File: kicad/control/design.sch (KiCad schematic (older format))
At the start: 20 parts, among them CON1 USB-MINI-B, IC1 ATMEGA1284P-P, P1 CONN_LH, P2 CONN_RH, P3 CONN_LT, P4 CONN_RT, P5 CONN_1, P6 CONN_1, SW1 RESET, X1 12 MHz

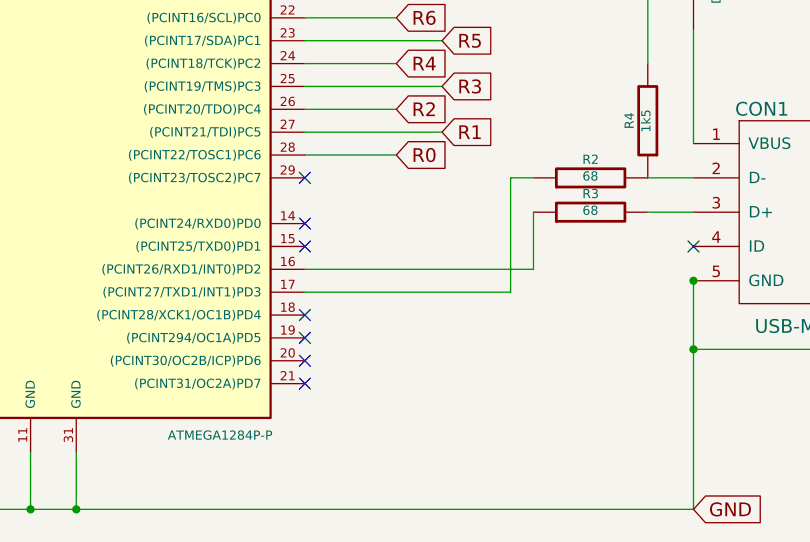
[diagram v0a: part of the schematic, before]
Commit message: adding logo to keypad
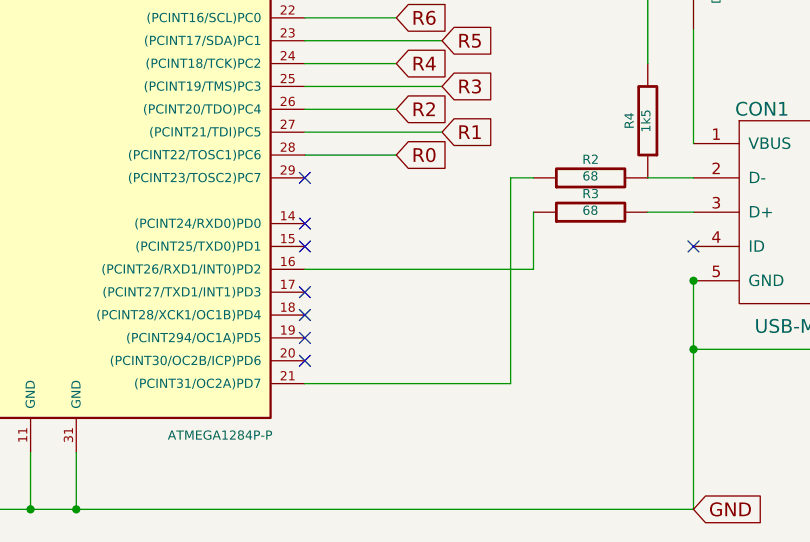
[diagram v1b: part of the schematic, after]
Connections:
- net at IC1.17 ((PCINT27/TXD1/INT1)PD3): no longer R2.1
- net at IC1.21 ((PCINT31/OC2A)PD7): now also R2.1
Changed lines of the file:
@@
 Sheet 1 1
 Title ""
-Date "11 feb 2014"
+Date "22 feb 2014"
 Rev ""
 Comp ""
@@
 Wire Wire Line
 	5450 5900 5450 5650
-Wire Wire Line
-	6650 4950 7550 4950
 $Comp
 L R R2
@@
 	7650 4450 7550 4450
 Wire Wire Line
-	7550 4450 7550 4950
+	7550 4450 7550 5350
 Text GLabel 10200 1550 0    60   Input ~ 0
 C0
@@
 NoConn ~ 6650 5150
 NoConn ~ 6650 5250
-NoConn ~ 6650 5350
 NoConn ~ 6650 4450
 NoConn ~ 6650 3550
@@
 NoConn ~ 6650 4650
 NoConn ~ 6650 4750
+Wire Wire Line
+	7550 5350 6650 5350
+NoConn ~ 6650 4950
 $EndSCHEMATC

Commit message: converting control to a Teensy
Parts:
- removed C1: 100nF, ~, symbol C
- removed C2: 4u7, ~, symbol CP1
- removed C3, C4: 20p, ~, symbol C
- removed CON1: USB-MINI-B, symbol USB-MINI-B
- removed D1, D2: DIODE, ~, symbol DIODE
- removed IC1: ATMEGA1284P-P, DIL40, symbol ATMEGA1284P-P
- removed R1: 10k, ~, symbol R
- removed R2, R3: 68, ~, symbol R
- removed R4: 1k5, ~, symbol R
- removed SW1: RESET, ~, symbol SW_PUSH
- removed X1: 12 MHz, ~, symbol CRYSTAL
- added P7: CONN_1, symbol CONN_1
- added U1: TEENSY2, symbol TEENSY2
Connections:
- net C0: now also U1.7 (D0)
- net C1: now also U1.8 (D1)
- net C2: now also P3.4, U1.9 (D2); no longer P3.2
- net C3: now also U1.10 (D3)
- net C4: now also P3.2, U1.23 (F0); no longer P3.4
- net C5: now also P4.4, U1.22 (F1); no longer P4.2
- net C6: now also U1.21 (F4)
- net C7: now also P4.2, U1.20 (F5); no longer P4.4
- net C8: now also U1.19 (F6)
- net C9: now also U1.18 (F7)
- net GND: now also P7.1, U1.1 (GND)
- net R0: now also U1.2 (B0)
- net R1: now also U1.3 (B1)
- net R2: now also U1.4 (B2)
- net R3: now also U1.5 (B3)
- net R4: now also U1.15 (B4)
- net R5: now also U1.16 (B5)
- net R6: now also U1.17 (B6)
- no-connect marks 14 -> 13

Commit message: generated output for seeedstudio order
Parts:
- added D1, D2, D3: LED, symbol LED
- added R1, R2, R3: 500, symbol R
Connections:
- net GND: now also R1.2, R2.2, R3.2
- net L0: now reaches U1.11 (C6)
- net L0: now also D1.1 (A)
- net L1: now reaches U1.12 (C7)
- net L1: now also D2.1 (A)
- net L2: now reaches U1.13 (D6)
- net L2: now also D3.1 (A)
- new net: D1.2 (K), R1.1
- new net: D2.2 (K), R2.1
- new net: D3.2 (K), R3.1
- no-connect marks 13 -> 10
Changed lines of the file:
@@
 	4000 3700 4400 3700
 NoConn ~ 4400 3800
-NoConn ~ 5600 3700
-NoConn ~ 5600 3800
 NoConn ~ 5600 3100
 Wire Wire Line
@@
 NoConn ~ 4400 2600
 NoConn ~ 4400 2700
-NoConn ~ 4400 2800
-NoConn ~ 4400 2900
 $Comp
 L CONN_1 P5
@@
 $EndComp
 Connection ~ 4400 1300
+$Comp
+L LED D1
+U 1 1 531BA9B2
+P 4750 5350
+F 0 "D1" H 4750 5450 50  0000 C CNN
+F 1 "LED" H 4750 5250 50  0000 C CNN
+F 2 "" H 4750 5350 60  0000 C CNN
+F 3 "" H 4750 5350 60  0000 C CNN
+	1    4750 5350
+	0    1    1    0
+$EndComp
+$Comp
+L LED D2
+U 1 1 531BA9CE
+P 4900 5350
+F 0 "D2" H 4900 5450 50  0000 C CNN
+F 1 "LED" H 4900 5250 50  0000 C CNN
+F 2 "" H 4900 5350 60  0000 C CNN
+F 3 "" H 4900 5350 60  0000 C CNN
+	1    4900 5350
+	0    1    1    0
+$EndComp
+$Comp
+L LED D3
+U 1 1 531BA9D9
+P 5050 5350
+F 0 "D3" H 5050 5450 50  0000 C CNN
+F 1 "LED" H 5050 5250 50  0000 C CNN
+F 2 "" H 5050 5350 60  0000 C CNN
+F 3 "" H 5050 5350 60  0000 C CNN
+	1    5050 5350
+	0    1    1    0
+$EndComp
+Text GLabel 4000 2800 0    60   Input ~ 0
+L2
+Text GLabel 6000 3700 2    60   Input ~ 0
+L0
+Text GLabel 6200 3800 2    60   Input ~ 0
+L1
+Wire Wire Line
+	4000 2800 4400 2800
+Wire Wire Line
+	6000 3700 5600 3700
+Wire Wire Line
+	6200 3800 5600 3800
+Text GLabel 4750 5150 1    60   Input ~ 0
+L0
+Text GLabel 4900 5150 1    60   Input ~ 0
+L1
+Text GLabel 5050 5150 1    60   Input ~ 0
+L2
+$Comp
+L R R1
+U 1 1 531BB4DC
+P 4750 5800
+F 0 "R1" V 4830 5800 40  0000 C CNN
+F 1 "500" V 4757 5801 40  0000 C CNN
+F 2 "" V 4680 5800 30  0000 C CNN
+F 3 "" H 4750 5800 30  0000 C CNN
+	1    4750 5800
+	1    0    0    -1
+$EndComp
+$Comp
+L R R2
+U 1 1 531BB4EE
+P 4900 5800
+F 0 "R2" V 4980 5800 40  0000 C CNN
+F 1 "500" V 4907 5801 40  0000 C CNN
+F 2 "" V 4830 5800 30  0000 C CNN
+F 3 "" H 4900 5800 30  0000 C CNN
+	1    4900 5800
+	1    0    0    -1
+$EndComp
+$Comp
+L R R3
+U 1 1 531BB4F9
+P 5050 5800
+F 0 "R3" V 5130 5800 40  0000 C CNN
+F 1 "500" V 5057 5801 40  0000 C CNN
+F 2 "" V 4980 5800 30  0000 C CNN
+F 3 "" H 5050 5800 30  0000 C CNN
+	1    5050 5800
+	1    0    0    -1
+$EndComp
+Text GLabel 4600 6200 0    60   Input ~ 0
+GND
+Wire Wire Line
+	4750 6200 4750 6050
+Wire Wire Line
+	4900 6200 4900 6050
+Connection ~ 4750 6200
+Wire Wire Line
+	5050 6200 5050 6050
+Connection ~ 4900 6200
+Connection ~ 5050 6200
+Wire Wire Line
+	4600 6200 5050 6200
+NoConn ~ 4400 2900
 $EndSCHEMATC
